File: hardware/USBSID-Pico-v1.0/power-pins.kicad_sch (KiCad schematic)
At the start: 42 parts, among them J10 BP, J12 12v/9v, J13 A5, J14 UART, J15 BP, U2 MT3608, U3 MT3608

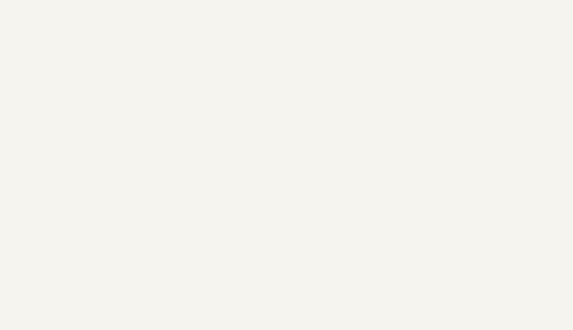
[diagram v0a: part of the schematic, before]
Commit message: Update v1.0 pcb with OSHWA certification
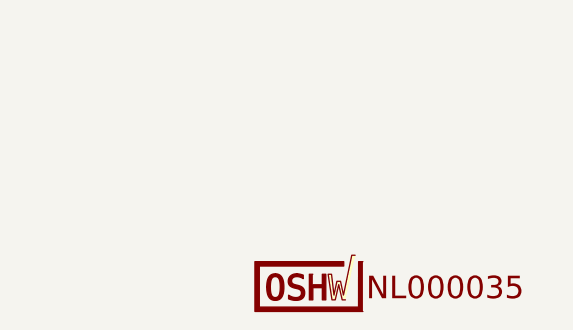
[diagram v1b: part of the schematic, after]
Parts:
- added LOGO2: ~, symbol OSHW_Certification_Mark:OSHW_US10_Certification_Mark_Wide_Medium
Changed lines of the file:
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@@
+	)
+	(symbol
+		(lib_id "OSHW_Certification_Mark:OSHW_US10_Certification_Mark_Wide_Medium")
+		(at 222.25 173.99 0)
+		(unit 1)
+		(exclude_from_sim no)
+		(in_bom no)
+		(on_board no)
+		(dnp no)
+		(fields_autoplaced yes)
+		(property "Reference" "LOGO2"
+			(at 222.25 173.99 0)
+			(effects
+				(font
+					(size 1.27 1.27)
+				)
+				(hide yes)
+			)
+		)
+		(property "Value" "~"
+			(at 222.25 173.99 0)
+			(effects
+				(font
+					(size 1.27 1.27)
+				)
+				(hide yes)
+			)
+		)
+		(property "Footprint" ""
+			(at 222.25 173.99 0)
+			(effects
+				(font
+					(size 1.27 1.27)
+				)
+				(hide yes)
+			)
+		)
+		(property "Datasheet" ""
+			(at 222.25 173.99 0)
+			(effects
+				(font
+					(size 1.27 1.27)
+				)
+				(hide yes)
+			)
+		)
+		(property "Description" "OSHW Certification Mark, Wide"
+			(at 222.25 173.99 0)
+			(effects
+				(font
+					(size 1.27 1.27)
+				)
+				(hide yes)
+			)
+		)
+		(instances
+			(project "USBSID-Pico-v1.0"
+				(path "/f639dbf8-eb43-4301-9a54-898621165136/c9a14a99-dfb1-4bad-b2ea-e0147bbc5de2"
+					(reference "LOGO2")
+					(unit 1)
+				)
+			)
+		)
 	)
 	(symbol
